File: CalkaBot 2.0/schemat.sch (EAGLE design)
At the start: 36 parts, among them IC1 TB6612FNG, IC2 LM339D, Q1 16MHz

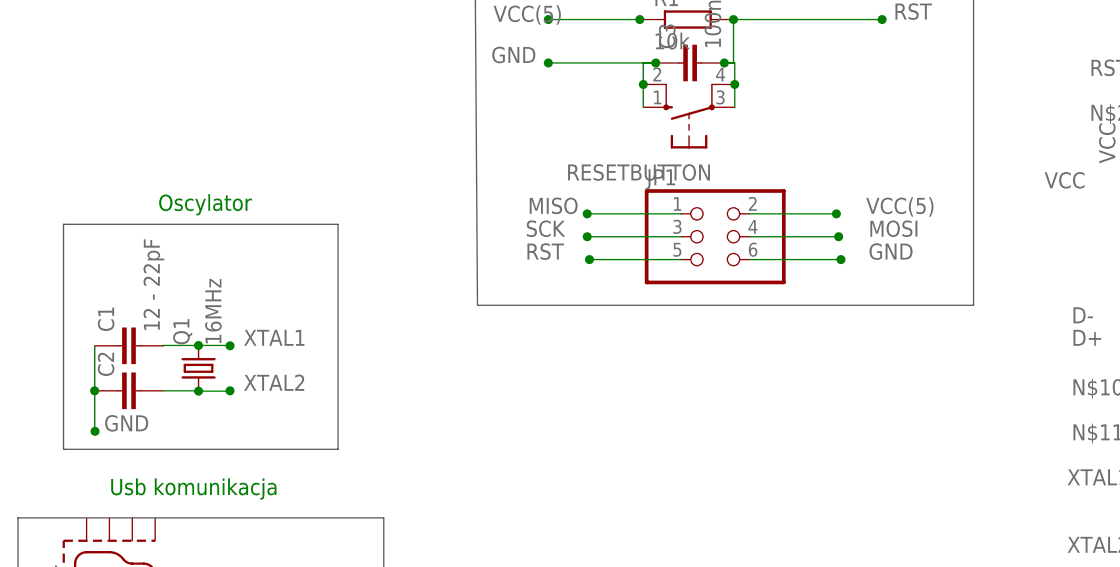
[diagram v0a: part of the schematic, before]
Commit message: added resonator
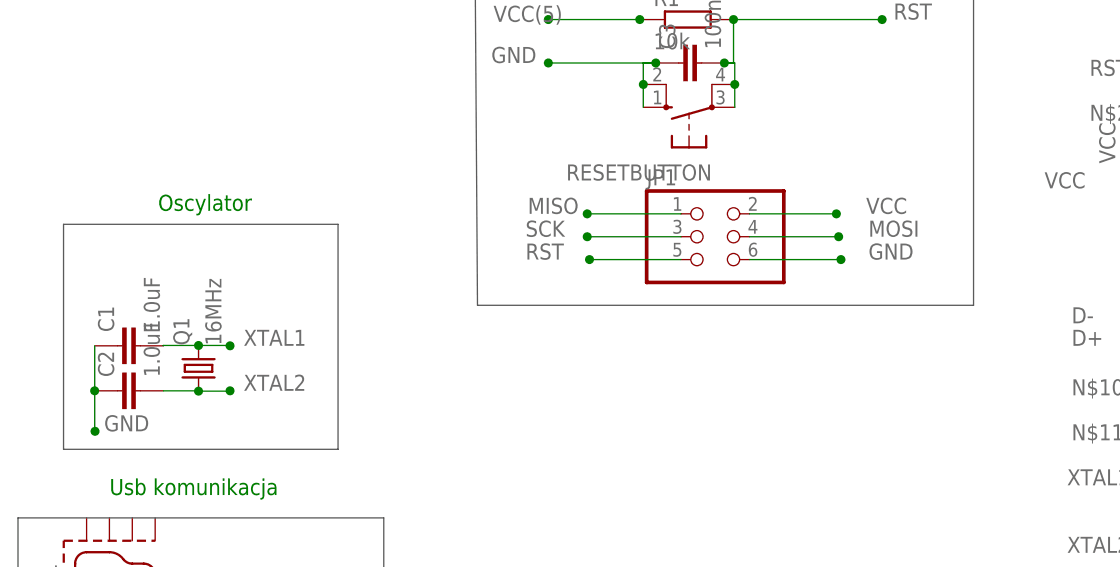
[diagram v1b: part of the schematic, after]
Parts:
- C1: value 12 - 22pF -> 1.0uF; device capacitor-wima:C5/3 -> rcl:C-EUC0805
- C2: value (none) -> 1.0uF; device capacitor-wima:C5/3 -> rcl:C-EUC0805
- Q1: device crystal:CRYSTALHC33U-V -> crystal:CSM-7X-DU
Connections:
- net VCC: now also JP1.2
- net VCC(5): no longer JP1.2
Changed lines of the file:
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@@
 <layer number="112" name="tSilk" color="7" fill="1" visible="no" active="yes"/>
 <layer number="113" name="ReferenceLS" color="7" fill="1" visible="no" active="no"/>
+<layer number="114" name="Badge_Outline" color="7" fill="1" visible="yes" active="yes"/>
+<layer number="115" name="ReferenceISLANDS" color="7" fill="1" visible="yes" active="yes"/>
 <layer number="116" name="Patch_BOT" color="9" fill="4" visible="no" active="yes"/>
 <layer number="118" name="Rect_Pads" color="7" fill="1" visible="no" active="no"/>
@@
 <part name="IC1" library="adafruit" deviceset="TB6612FNG" device=""/>
 <part name="U$1" library="adafruit" deviceset="ATMEGA32U4" device="-AU"/>
-<part name="Q1" library="crystal" library_urn="urn:adsk.eagle:library:204" deviceset="CRYSTAL" device="HC33U-V" package3d_urn="urn:adsk.eagle:package:12084/1" value="16MHz"/>
-<part name="C1" library="capacitor-wima" library_urn="urn:adsk.eagle:library:116" deviceset="C" device="5/3" package3d_urn="urn:adsk.eagle:package:5433/1" value="12 - 22pF"/>
-<part name="C2" library="capacitor-wima" library_urn="urn:adsk.eagle:library:116" deviceset="C" device="5/3" package3d_urn="urn:adsk.eagle:package:5433/1"/>
+<part name="Q1" library="crystal" library_urn="urn:adsk.eagle:library:204" deviceset="CSM-7X-DU" device="" package3d_urn="urn:adsk.eagle:package:12105/1" value="16MHz"/>
+<part name="C1" library="rcl" library_urn="urn:adsk.eagle:library:334" deviceset="C-EU" device="C0805" package3d_urn="urn:adsk.eagle:package:23617/2" value="1.0uF"/>
+<part name="C2" library="rcl" library_urn="urn:adsk.eagle:library:334" deviceset="C-EU" device="C0805" package3d_urn="urn:adsk.eagle:package:23617/2" value="1.0uF"/>
 <part name="U$2" library="con-molex-usb" deviceset="MICRO-USB-RECEPTACLE" device="47589-0001"/>
 <part name="JP1" library="pinhead" library_urn="urn:adsk.eagle:library:325" deviceset="PINHD-2X3" device="" package3d_urn="urn:adsk.eagle:package:22462/2"/>
@@
 <instance part="IC1" gate="G$1" x="92" y="64"/>
 <instance part="U$1" gate="G$1" x="-10" y="62"/>
-<instance part="Q1" gate="G$1" x="-142.5" y="72.5" rot="R90"/>
+<instance part="Q1" gate="P" x="-142.5" y="72.5" rot="R90"/>
 <instance part="C1" gate="G$1" x="-151.5" y="75" rot="R90"/>
 <instance part="C2" gate="G$1" x="-151.5" y="70" rot="R90"/>
@@
 </segment>
 <segment>
-<pinref part="JP1" gate="A" pin="2"/>
-<wire x1="-81.28" y1="89.662" x2="-71.628" y2="89.662" width="0.1524" layer="91"/>
-<wire x1="-71.628" y1="89.662" x2="-71.628" y2="89.408" width="0.1524" layer="91"/>
-<junction x="-71.628" y="89.662"/>
-<label x="-68.326" y="89.662" size="1.778" layer="95"/>
-</segment>
-<segment>
 <wire x1="-103.632" y1="111.252" x2="-93.472" y2="111.252" width="0.1524" layer="91"/>
 <junction x="-103.632" y="111.252"/>
@@
 </segment>
 <segment>
-<pinref part="Q1" gate="G$1" pin="2"/>
+<pinref part="Q1" gate="P" pin="2"/>
 <wire x1="-142.5" y1="75.04" x2="-139" y2="75.04" width="0.1524" layer="91"/>
 <wire x1="-139" y1="75.04" x2="-139" y2="75" width="0.1524" layer="91"/>
@@
 </segment>
 <segment>
-<pinref part="Q1" gate="G$1" pin="1"/>
+<pinref part="Q1" gate="P" pin="1"/>
 <wire x1="-142.5" y1="69.96" x2="-139" y2="69.96" width="0.1524" layer="91"/>
 <wire x1="-139" y1="69.96" x2="-139" y2="70" width="0.1524" layer="91"/>
@@
 <wire x1="-32.86" y1="95.26" x2="-32.86" y2="92.48" width="0.1524" layer="91"/>
 </segment>
-</net>
+<segment>
+<pinref part="JP1" gate="A" pin="2"/>
+<wire x1="-81.28" y1="89.662" x2="-71.628" y2="89.662" width="0.1524" layer="91"/>
+<wire x1="-71.628" y1="89.662" x2="-71.628" y2="89.408" width="0.1524" layer="91"/>
+<junction x="-71.628" y="89.662"/>
+<label x="-68.326" y="89.662" size="1.778" layer="95"/>
+</segment>
+</net>

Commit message: Powiększone dziurki
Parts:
- renumbered R2 to POT
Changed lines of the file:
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@@
 <setting verticaltext="up"/>
 </settings>
-<grid distance="0.1" unitdist="inch" unit="inch" style="lines" multiple="1" display="no" altdistance="0.01" altunitdist="inch" altunit="inch"/>
+<grid distance="10" unitdist="mil" unit="mil" style="lines" multiple="1" display="no" altdistance="0.01" altunitdist="inch" altunit="inch"/>
 <layers>
 <layer number="1" name="Top" color="4" fill="1" visible="no" active="no"/>
@@
 <part name="RESETBUTTON" library="switch-omron" library_urn="urn:adsk.eagle:library:377" deviceset="10-XX" device="" package3d_urn="urn:adsk.eagle:package:27496/1"/>
 <part name="IC2" library="linear" deviceset="LM339" device="D"/>
-<part name="R2" library="pot" library_urn="urn:adsk.eagle:library:331" deviceset="TRIM_EU-" device="CA6V" package3d_urn="urn:adsk.eagle:package:22691/1" value="100k"/>
+<part name="POT" library="pot" library_urn="urn:adsk.eagle:library:331" deviceset="TRIM_EU-" device="CA6V" package3d_urn="urn:adsk.eagle:package:22691/1" value="100k"/>
 <part name="GND1" library="supply1" library_urn="urn:adsk.eagle:library:371" deviceset="GND" device=""/>
 <part name="P+1" library="supply1" library_urn="urn:adsk.eagle:library:371" deviceset="VCC" device=""/>
@@
 <part name="P+20" library="supply1" library_urn="urn:adsk.eagle:library:371" deviceset="VCC" device=""/>
 <part name="P+5" library="supply1" library_urn="urn:adsk.eagle:library:371" deviceset="VCC" device=""/>
+<part name="GND4" library="supply1" library_urn="urn:adsk.eagle:library:371" deviceset="GND" device=""/>
 </parts>
 <sheets>
@@
 <instance part="IC2" gate="C" x="227" y="33.8"/>
 <instance part="IC2" gate="D" x="223.2" y="-7.2"/>
-<instance part="R2" gate="1" x="186.3" y="87" rot="R90"/>
+<instance part="POT" gate="1" x="186.3" y="87" rot="R90"/>
 <instance part="GND1" gate="1" x="191.5" y="84.2"/>
 <instance part="P+1" gate="VCC" x="181.2" y="91.3"/>
@@
 <instance part="P+20" gate="VCC" x="235.7" y="20.8"/>
 <instance part="P+5" gate="VCC" x="-38.1" y="97.8"/>
+<instance part="GND4" gate="1" x="70.866" y="69.85"/>
 </instances>
 <busses>
@@
 </segment>
 <segment>
-<pinref part="R2" gate="1" pin="A"/>
+<pinref part="POT" gate="1" pin="A"/>
 <pinref part="GND1" gate="1" pin="GND"/>
 <wire x1="191.38" y1="87" x2="191.38" y2="86.74" width="0.1524" layer="91"/>
@@
 <wire x1="197.42" y1="-10.14" x2="198.9" y2="-10.14" width="0.1524" layer="91"/>
 <wire x1="198.9" y1="-10.14" x2="198.9" y2="-11.06" width="0.1524" layer="91"/>
+</segment>
+<segment>
+<wire x1="74.168" y1="74.168" x2="70.866" y2="74.168" width="0.1524" layer="91"/>
+<wire x1="70.866" y1="74.168" x2="70.866" y2="73.66" width="0.1524" layer="91"/>
+<wire x1="70.866" y1="73.66" x2="70.866" y2="72.39" width="0.1524" layer="91"/>
+<wire x1="74.168" y1="76.708" x2="70.866" y2="76.708" width="0.1524" layer="91"/>
+<wire x1="70.866" y1="76.708" x2="70.866" y2="74.168" width="0.1524" layer="91"/>
+<pinref part="GND4" gate="1" pin="GND"/>
 </segment>
 </net>
@@
 <segment>
 <pinref part="P+1" gate="VCC" pin="VCC"/>
-<pinref part="R2" gate="1" pin="E"/>
+<pinref part="POT" gate="1" pin="E"/>
 <wire x1="181.2" y1="88.76" x2="181.2" y2="87" width="0.1524" layer="91"/>
 <wire x1="181.2" y1="87" x2="181.22" y2="87" width="0.1524" layer="91"/>
@@
 <net name="POT" class="0">
 <segment>
-<pinref part="R2" gate="1" pin="S"/>
+<pinref part="POT" gate="1" pin="S"/>
 <wire x1="186.3" y1="92.08" x2="192.68" y2="92.08" width="0.1524" layer="91"/>
 <label x="194.3" y="92.1" size="1.778" layer="95"/>

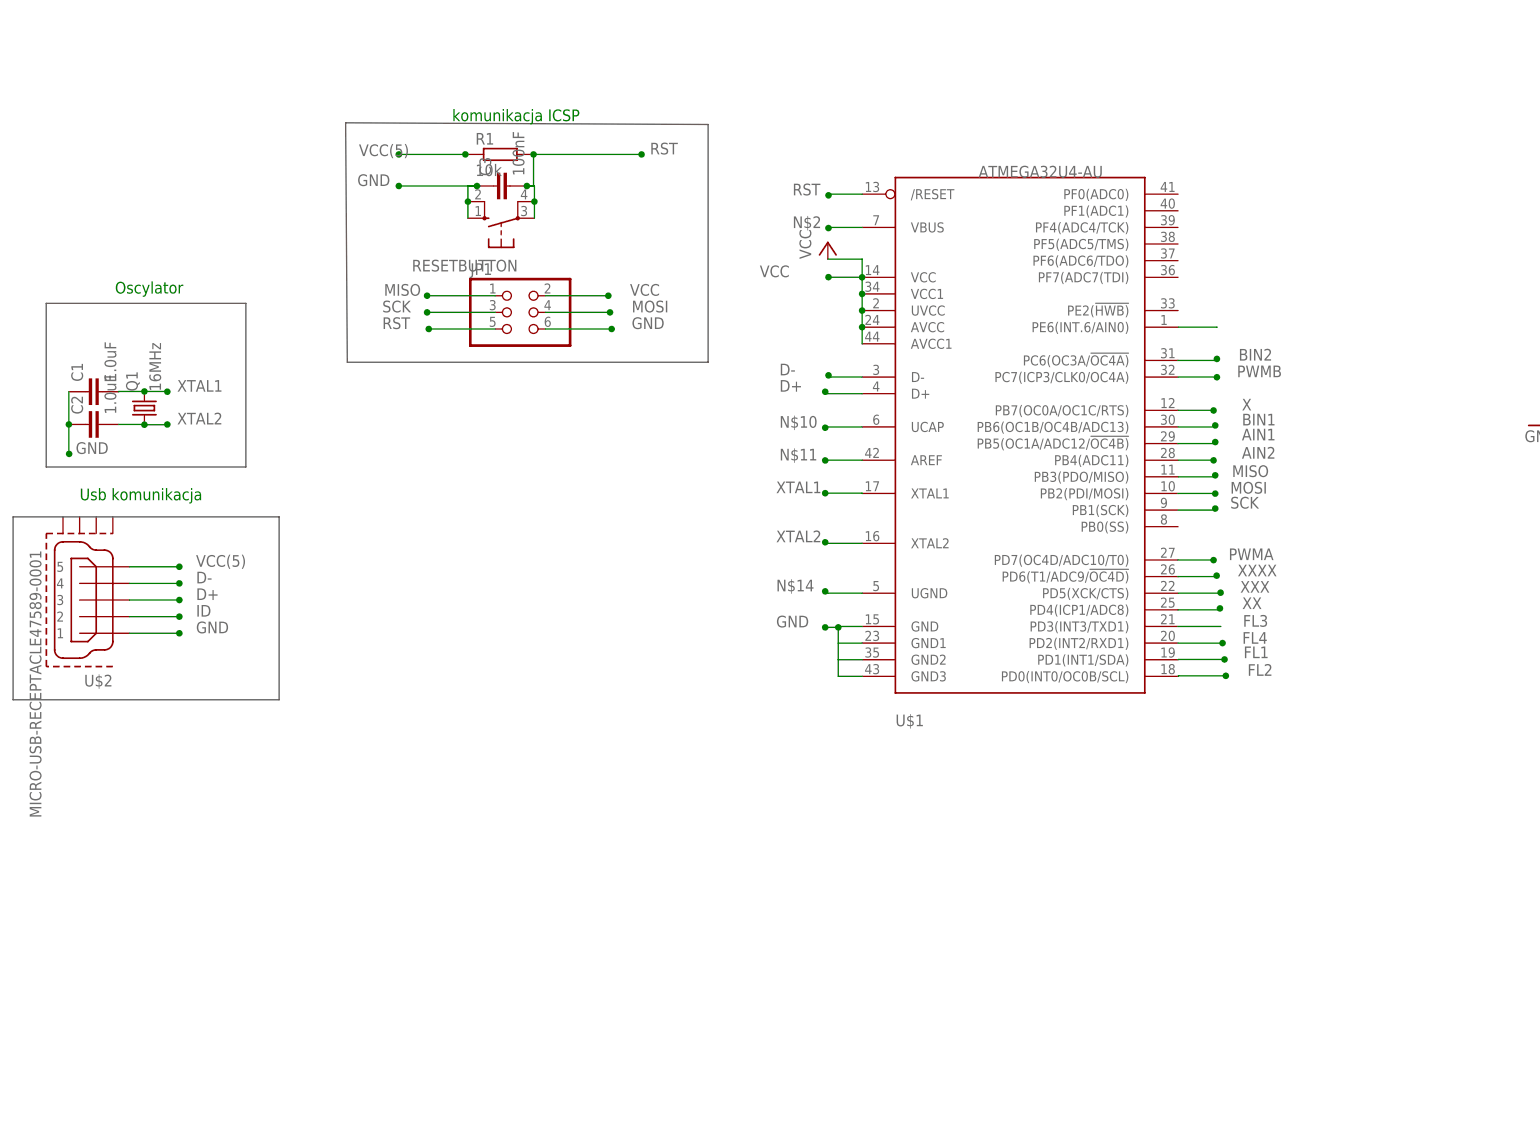
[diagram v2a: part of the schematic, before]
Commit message: przyciski i usunalem isp
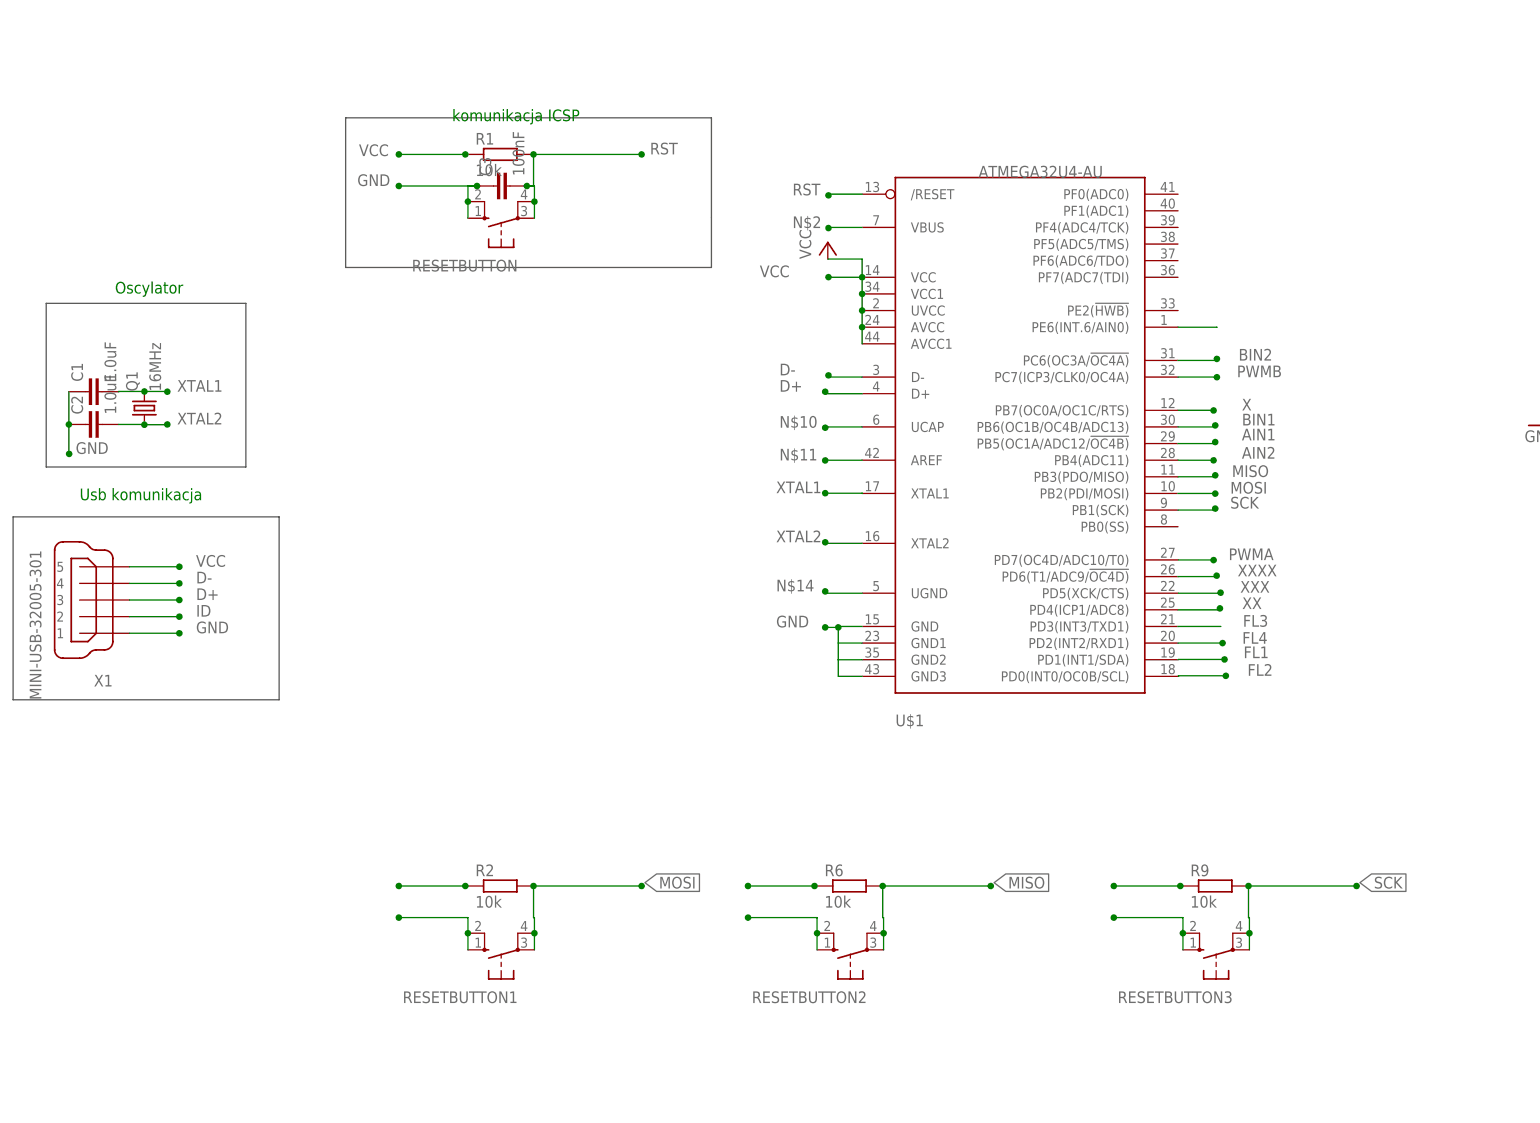
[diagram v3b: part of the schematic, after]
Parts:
- removed JP1: (no value), pinhead:PINHD-2X3
- removed U$2: MICRO-USB-RECEPTACLE47589-0001, con-molex-usb:MICRO-USB-RECEPTACLE47589-0001
- added R2, R6, R9: 10k, rcl:R-EU_R0805
- added RESETBUTTON1, RESETBUTTON2, RESETBUTTON3: (no value), switch-omron:10-XX
- added X1: MINI-USB-32005-301, con-cypressindustries:MINI-USB-32005-301
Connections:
- removed net VCC(5): R1.1, U$2.5
- new net GND2: RESETBUTTON2.S, RESETBUTTON2.S1
- new net GND3: RESETBUTTON3.S, RESETBUTTON3.S1
- new net VCC2: R6.1
- new net VCC3: R9.1
- net D+: now also X1.3; no longer U$2.3
- net D-: now also X1.4; no longer U$2.4
- net GND: now also RESETBUTTON1.S, RESETBUTTON1.S1, X1.1; no longer JP1.6, U$2.1
- net ID: now also X1.2; no longer U$2.2
- net MISO: now also R6.2, RESETBUTTON2.P, RESETBUTTON2.P1; no longer JP1.1
- net MOSI: now also R2.2, RESETBUTTON1.P, RESETBUTTON1.P1; no longer JP1.4
- net RST: no longer JP1.5
- net SCK: now also R9.2, RESETBUTTON3.P, RESETBUTTON3.P1; no longer JP1.3
- net VCC: now also R1.1, R2.1, X1.5; no longer JP1.2

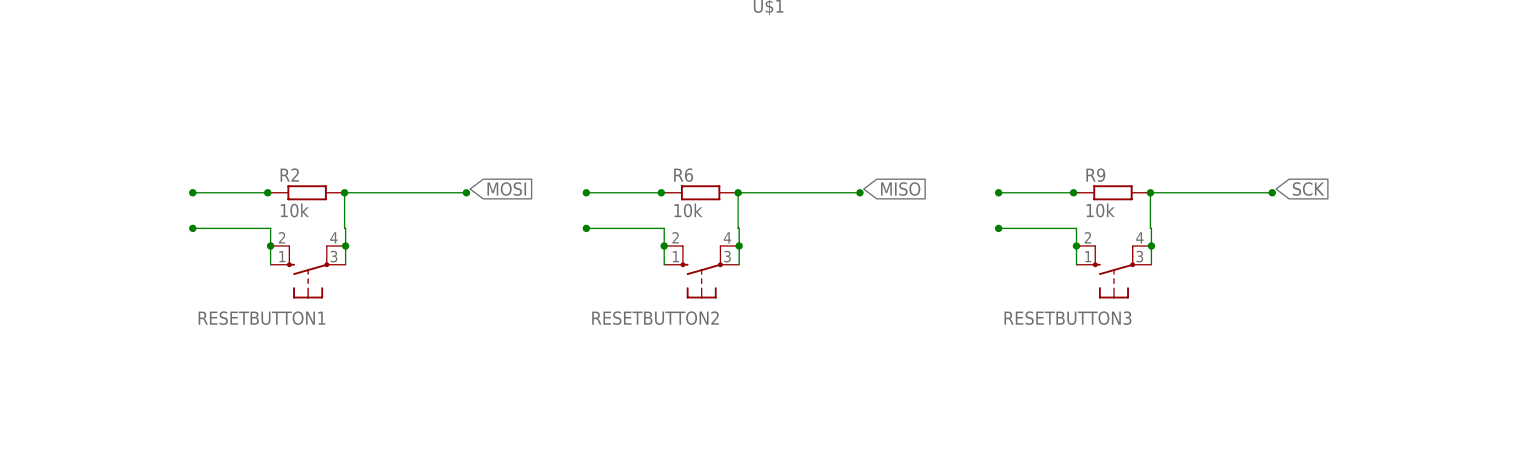
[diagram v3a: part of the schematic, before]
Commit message: Dodałem stabilizator i filtrację stabilizator i przyciski
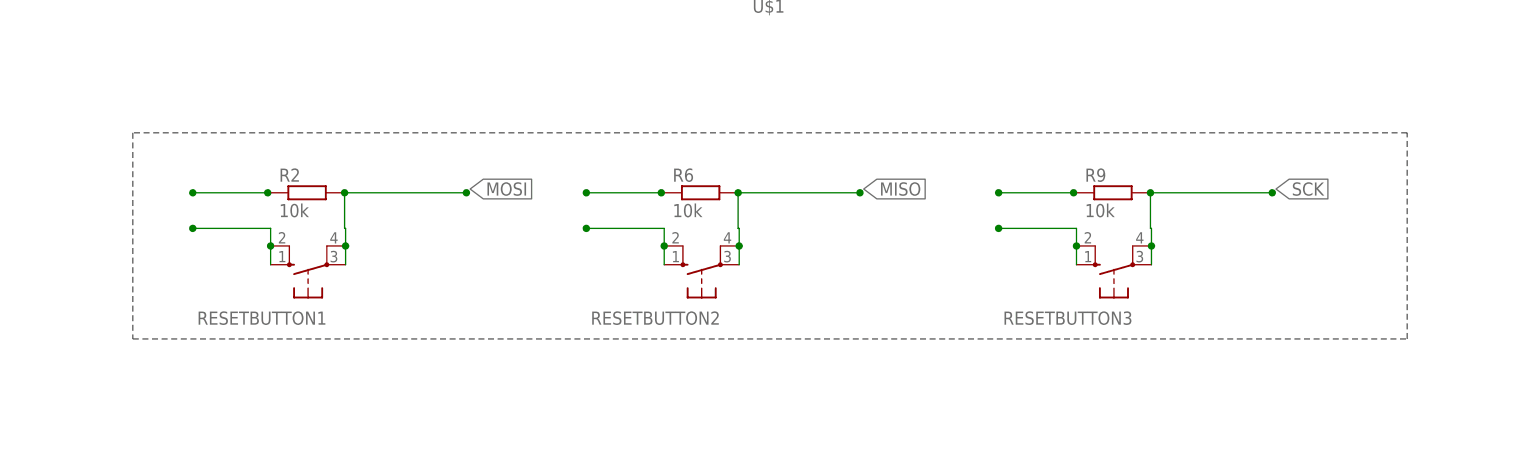
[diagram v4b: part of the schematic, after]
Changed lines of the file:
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@@
+</segment>
+</bus>
+<bus name="B$3">
+<segment>
+<wire x1="-111.76" y1="7.62" x2="-111.76" y2="-20.32" width="0.762" layer="92" style="shortdash"/>
+<wire x1="-111.76" y1="-20.32" x2="60.96" y2="-20.32" width="0.762" layer="92" style="shortdash"/>
+<wire x1="60.96" y1="-20.32" x2="60.96" y2="7.62" width="0.762" layer="92" style="shortdash"/>
+<wire x1="60.96" y1="7.62" x2="-111.76" y2="7.62" width="0.762" layer="92" style="shortdash"/>
 </segment>
 </bus>
